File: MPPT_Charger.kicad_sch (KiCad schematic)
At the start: 119 parts, among them J1 Solar, J2 Battery, J4 INTERFACE PORT, J6 JTAG, J8 Micro_SD_Card_Det_Hirose_DM3AT, J9 IIC RTC, P1 USB-C, Q1 CSD19505KCS, Q2 CSD19505KCS, Q3 CSD19505KCS, Q4 Si2306, Q5 MMBT3904 1A, Q6 MMBT3904 1A, Q7 Si2306, U1 ACS712, U10 ADS1015, U2 B1212S, U3 AMS1117-5.0, U4 AMS1117-3.3, U5 XL7005A, U6 XL7005A, U7 IR2104, U8 ESP32, U9 CH340G

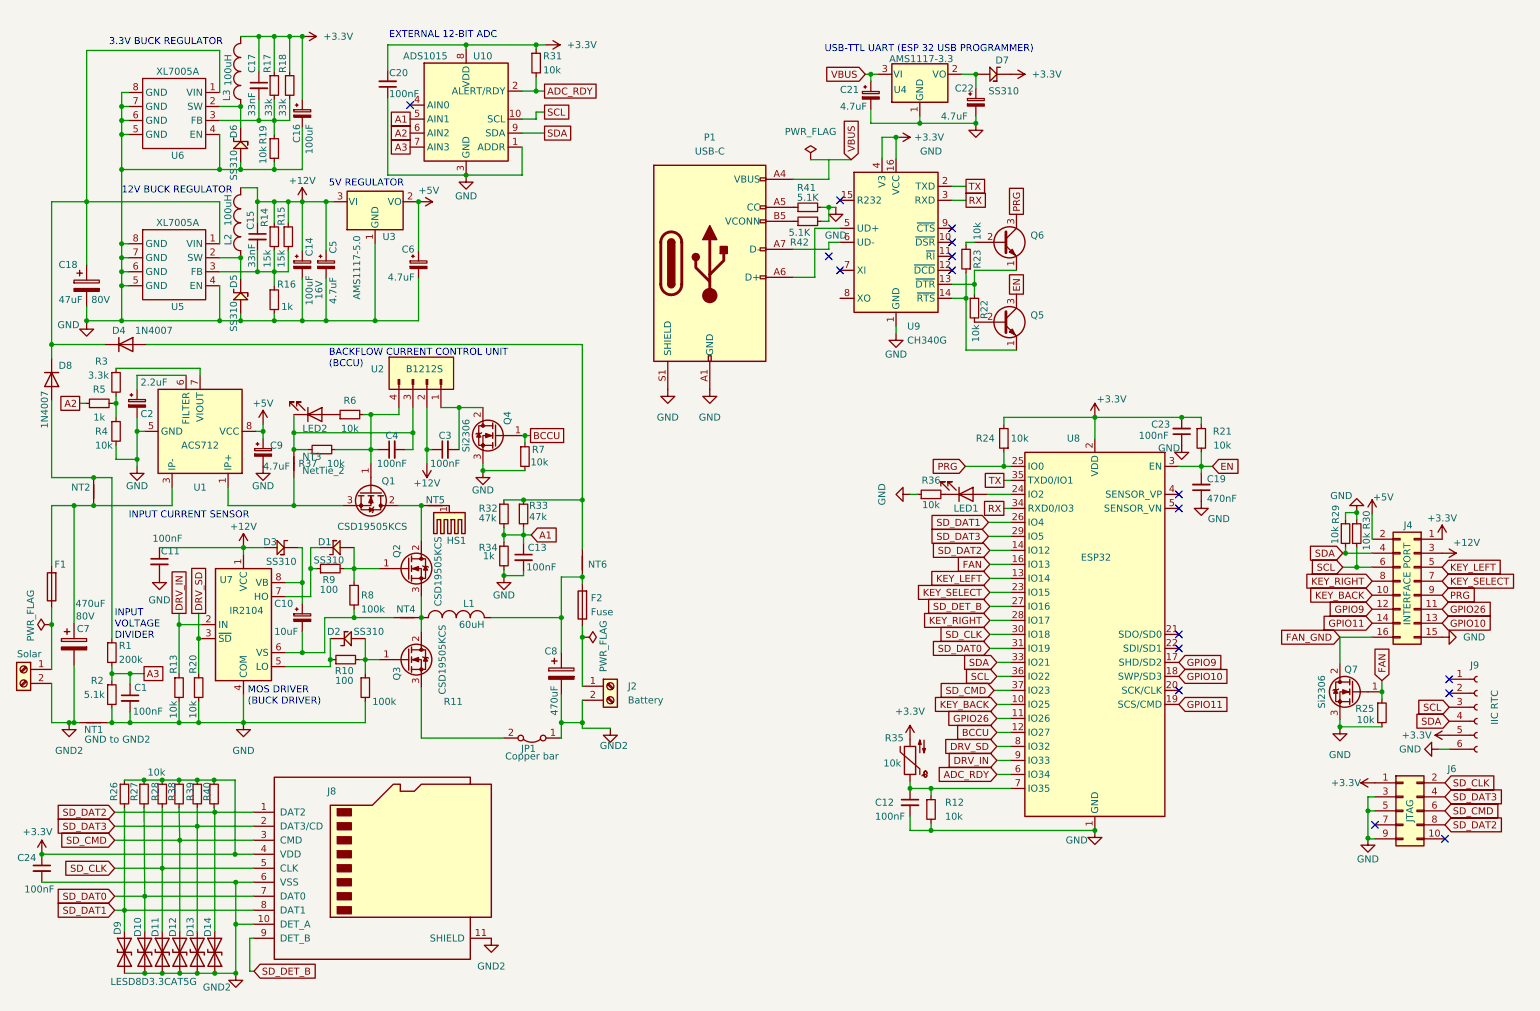
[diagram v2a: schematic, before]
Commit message: A lot of updates. Used net classes. Changed some footprints and 3D models. Corrected pinouts of connectors. Changed pins for keyboard to use same pins as JTAG connector, seemed like a useful double use that should not collide, and I am running out of GPIOs soon.
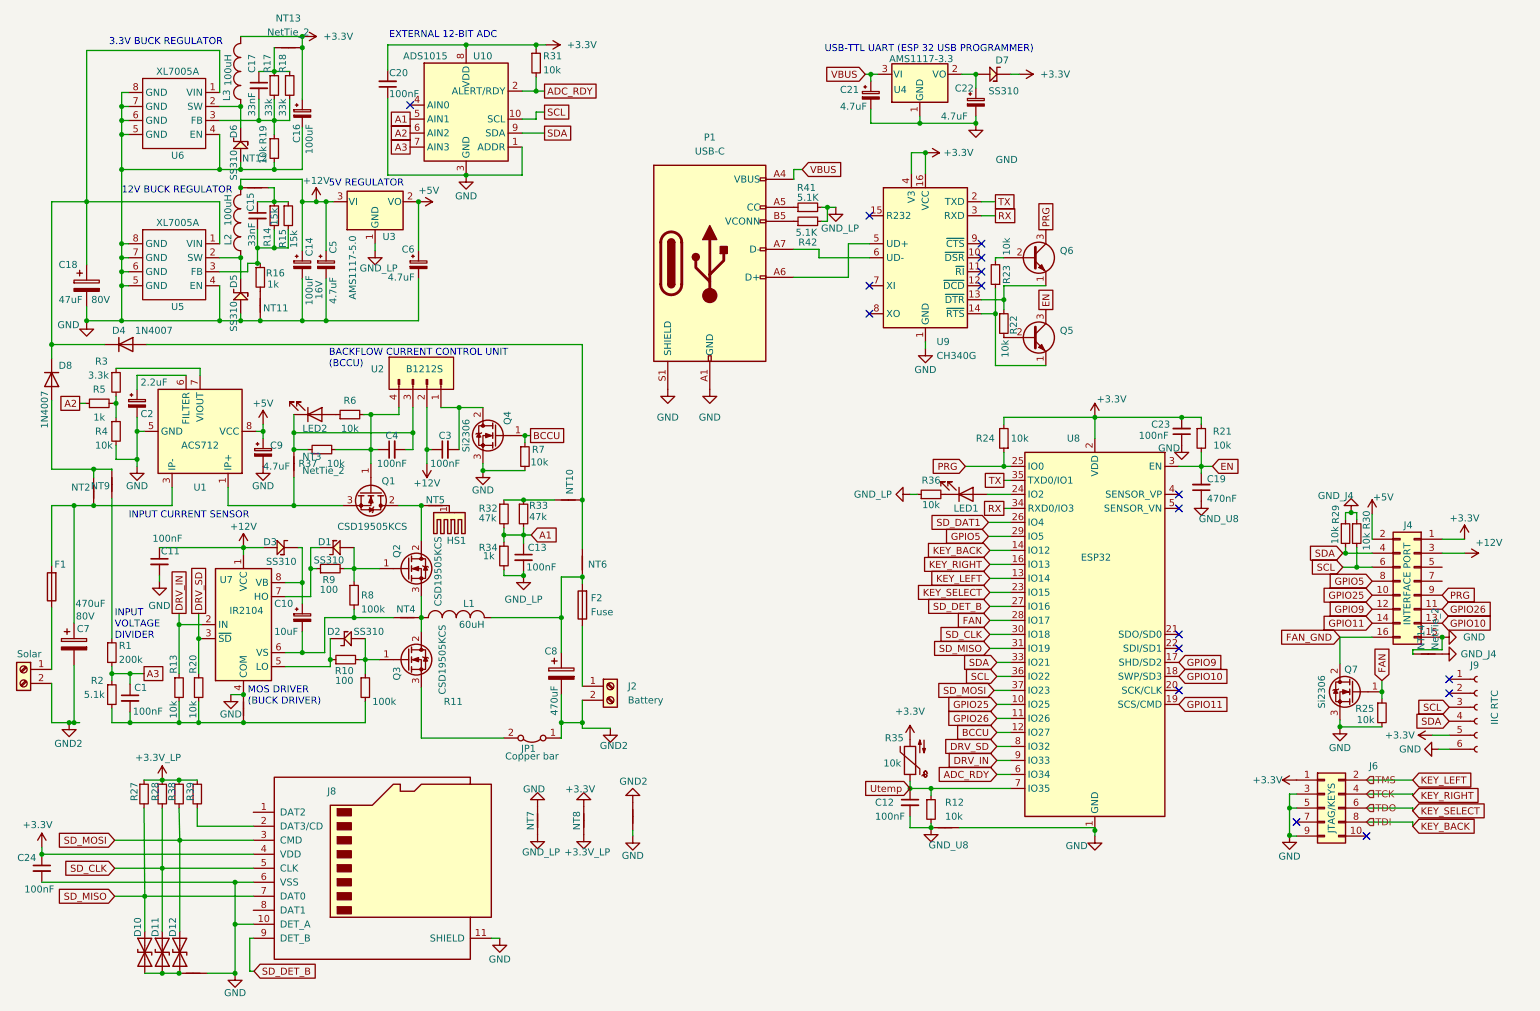
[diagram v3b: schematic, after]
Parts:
- removed D13, D14, D9: LESD8D3.3CAT5G, AA:SOD882D.kicad_mod, symbol Diode:1N62xxCA
- removed R26, R40: 10k, Resistor_SMD:R_0603_1608Metric, symbol Device:R_Small
- added NT10, NT11, NT12, NT13, NT14, NT15, NT16, NT17, NT9: NetTie_2, NetTie:NetTie-2_SMD_Pad0.5mm, symbol Device:NetTie_2
- added NT7, NT8: ~, NetTie:NetTie-2_SMD_Pad0.5mm, symbol Device:NetTie_2
- C1: JLCPCB Part (none) -> C14663 CC0603KRX7R9BB104
- C17: LCSC (none) -> C21117 CL10B333KB8NNNC; Voltage (none) -> 5V
- C6: LCSC (none) -> C1779 CL21A475KAQNNNE; Voltage (none) -> 5V
- C8: Voltage (none) -> 50V
- D4, D8: footprint Diode_SMD:D_SMB -> Diode_SMD:D_SOD-123F
- J6: value JTAG -> JTAG/KEYS
- U1: LCSC (none) -> C10681 ACS712ELCTR-20A-T
- U9: LCSC (none) -> C14267 CH340G
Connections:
- net +12V: now also NT12.1; no longer C15.1, R14.1, R15.1
- net +3.3V: now also NT13.2, NT8.2; no longer C17.1, R17.1, R18.1, R27.1, R28.1, R38.1, R39.1
- net FAN: now also U8.28 (IO17); no longer U8.16 (IO13)
- net GND: now also C24.2, J8.10 (DET_A), J8.11 (SHIELD), J8.6 (VSS), NT1.2, NT11.1, NT14.2, NT15.2, NT16.2, NT17.2, NT7.2; no longer C1.2, C12.2, C13.2, C19.1, NT1.1, R11.2, R12.2, R13.2, R16.2, R2.2, R20.2, R29.1, R30.1, R34.2, R36.1, R41.2, R42.2, U3.1 (GND)
- net GND2: now also NT1.1; no longer C24.2, D10.1 (A1), D11.1 (A1), D12.1 (A1), J8.10 (DET_A), J8.11 (SHIELD), J8.6 (VSS), NT1.2
- net KEY_BACK: now also J6.8 (Pin_8), U8.14 (IO12); no longer J4.10 (Pin_10), U8.10 (IO25)
- net KEY_LEFT: now also J6.2 (Pin_2); no longer J4.5 (Pin_5)
- net KEY_RIGHT: now also J6.4 (Pin_4), U8.16 (IO13); no longer J4.8 (Pin_8), U8.28 (IO17)
- net KEY_SELECT: now also J6.6 (Pin_6); no longer J4.7 (Pin_7)
- net SD_CLK: no longer J6.2 (Pin_2)
- net SD_DAT1: no longer J8.8 (DAT1)
- net VBUS: now also P1.A4 (VBUS), P1.A9 (VBUS), P1.B4 (VBUS), P1.B9 (VBUS)
- net Utemp: now reaches C12.1, R12.1, R35.1, U8.7 (IO35)
- net at D8.2 (A), NT2.1: now also NT9.1; no longer R1.1
- net at R32.1, R33.1: now also NT10.2; no longer D4.2 (A), NT6.2
- net SD_CMD renamed SD_MOSI
- net SD_MOSI: no longer J6.6 (Pin_6)
- net SD_DAT0 renamed SD_MISO
- removed net SD_DAT2: J6.8 (Pin_8), J8.1 (DAT2), U8.14 (IO12)
- net SD_DAT3: no longer names the net of J8.2 (DAT3/CD), R39.2
- net SD_DAT3: no longer J6.4 (Pin_4), U8.29 (IO5)
- new net: C1.2, NT17.1, R11.2, R13.2, R2.2, R20.2
- new net: C17.1, NT13.1, R17.1, R18.1
- new net: NT11.2, R16.2
- new net: C15.1, NT12.2, R14.1, R15.1
- new net: D10.1 (A1), D11.1 (A1), D12.1 (A1), NT16.1
- new net: D4.2 (A), NT10.1, NT6.2
- new net: NT9.2, R1.1
- new net +3.3V_LP: NT8.1, R27.1, R28.1, R38.1, R39.1
- new net GND_J4: NT14.1, R29.1, R30.1
- new net GND_LP: C13.2, NT7.1, R34.2, R36.1, R41.2, R42.2, U3.1 (GND)
- new net GND_U8: C12.2, C19.1, NT15.1, R12.2
- new net GPIO25: J4.10 (Pin_10), U8.10 (IO25)
- new net GPIO5: J4.8 (Pin_8), U8.29 (IO5)
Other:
- moved on the sheet: C15, J6, Q5, Q6, R14, R15, R16, R22, R23, U9

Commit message: Some Zones were wrong/missing
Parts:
- NT3: value NetTie_2 -> ~
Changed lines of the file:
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@@
 	)
 	(junction
-		(at 24.384 139.192)
-		(diameter 0)
-		(color 0 0 0 0)
-	)
-	(junction
 		(at 116.586 139.192)
 		(diameter 0)
@@
 	(wire
 		(pts
+			(xy 108.458 153.67) (xy 108.458 154.432)
+		)
+		(stroke
+			(width 0)
+			(type default)
+		)
+	)
+	(wire
+		(pts
 			(xy 65.786 44.704) (xy 65.786 53.594)
 		)
@@
 	(wire
 		(pts
+			(xy 125.73 159.258) (xy 125.73 159.766)
+		)
+		(stroke
+			(width 0)
+			(type default)
+		)
+	)
+	(wire
+		(pts
 			(xy 70.866 127.762) (xy 71.12 127.762)
 		)
@@
 	(wire
 		(pts
-			(xy 24.384 139.192) (xy 25.4 139.192)
-		)
-		(stroke
-			(width 0)
-			(type default)
-		)
-	)
-	(wire
-		(pts
 			(xy 193.04 83.82) (xy 193.04 85.09)
 		)
@@
 	(wire
 		(pts
-			(xy 60.706 16.764) (xy 60.706 21.082)
+			(xy 116.84 153.67) (xy 116.84 154.432)
 		)
 		(stroke
@@
 	(wire
 		(pts
-			(xy 56.261 178.308) (xy 56.896 178.308)
+			(xy 60.706 16.764) (xy 60.706 21.082)
 		)
 		(stroke
@@
 	(wire
 		(pts
-			(xy 33.02 54.864) (xy 34.29 54.864)
+			(xy 56.261 178.308) (xy 56.896 178.308)
 		)
 		(stroke
@@
 	(wire
 		(pts
-			(xy 102.362 98.806) (xy 105.918 98.806)
+			(xy 33.02 54.864) (xy 34.29 54.864)
 		)
 		(stroke
@@
 	(wire
 		(pts
-			(xy 261.62 133.604) (xy 261.62 134.874)
+			(xy 102.362 98.806) (xy 105.918 98.806)
 		)
 		(stroke
@@
 	(wire
 		(pts
-			(xy 125.73 158.75) (xy 125.73 159.766)
+			(xy 261.62 133.604) (xy 261.62 134.874)
 		)
 		(stroke
@@
 	(wire
 		(pts
+			(xy 125.73 153.67) (xy 125.73 154.178)
+		)
+		(stroke
+			(width 0)
+			(type default)
+		)
+	)
+	(wire
+		(pts
 			(xy 65.786 126.492) (xy 69.85 126.492)
 		)
@@
 		(length 2.54)
 		(shape round)
-		(at 26.67 17.272 0)
+		(at 116.84 154.432 90)
 		(fields_autoplaced yes)
 		(effects
@@
 		)
 		(property "Netclass" "MEDPWR"
-			(at 27.3685 14.732 0)
+			(at 114.3 153.7335 90)
 			(show_name yes)
 			(effects
@@
 		(length 2.54)
 		(shape round)
-		(at 53.34 54.864 0)
+		(at 26.67 17.272 0)
 		(fields_autoplaced yes)
 		(effects
@@
 		)
 		(property "Netclass" "MEDPWR"
-			(at 54.0385 52.324 0)
+			(at 27.3685 14.732 0)
 			(show_name yes)
 			(effects
@@
 		(length 2.54)
 		(shape round)
-		(at 116.586 129.032 270)
+		(at 53.34 54.864 0)
 		(fields_autoplaced yes)
 		(effects
@@
 				(size 1.27 1.27)
 			)
-			(justify right bottom)
+			(justify left bottom)
 		)
-		(property "Netclass" "HIPWR"
-			(at 119.126 128.3335 90)
+		(property "Netclass" "MEDPWR"
+			(at 54.0385 52.324 0)
 			(show_name yes)
 			(effects
@@
 		(length 2.54)
 		(shape round)
-		(at 256.54 123.698 180)
+		(at 116.586 129.032 270)
 		(fields_autoplaced yes)
 		(effects
@@
 			(justify right bottom)
 		)
-		(property "Netclass" "MEDPWR"
-			(at 257.2385 126.238 0)
+		(property "Netclass" "HIPWR"
+			(at 119.126 128.3335 90)
 			(show_name yes)
 			(effects
@@
 		(length 2.54)
 		(shape round)
-		(at 25.908 93.218 0)
+		(at 256.54 123.698 180)
 		(fields_autoplaced yes)
 		(effects
@@
 				(size 1.27 1.27)
 			)
-			(justify left bottom)
+			(justify right bottom)
 		)
 		(property "Netclass" "MEDPWR"
-			(at 26.6065 90.678 0)
+			(at 257.2385 126.238 0)
 			(show_name yes)
 			(effects
@@
 		(length 2.54)
 		(shape round)
-		(at 87.376 116.84 90)
+		(at 25.908 93.218 0)
 		(fields_autoplaced yes)
 		(effects
@@
 			(justify left bottom)
 		)
-		(property "Netclass" "HIPWR"
-			(at 84.836 116.1415 90)
+		(property "Netclass" "MEDPWR"
+			(at 26.6065 90.678 0)
 			(show_name yes)
 			(effects
@@
 		(length 2.54)
 		(shape round)
-		(at 87.376 99.822 0)
+		(at 87.376 116.84 90)
 		(fields_autoplaced yes)
 		(effects
@@
 		)
 		(property "Netclass" "HIPWR"
-			(at 88.0745 97.282 0)
+			(at 84.836 116.1415 90)
 			(show_name yes)
 			(effects
@@
 		(length 2.54)
 		(shape round)
-		(at 273.558 105.918 0)
+		(at 87.376 99.822 0)
 		(fields_autoplaced yes)
 		(effects
@@
 			(justify left bottom)
 		)
-		(property "Netclass" "MEDPWR"
-			(at 274.2565 103.378 0)
+		(property "Netclass" "HIPWR"
+			(at 88.0745 97.282 0)
 			(show_name yes)
 			(effects
@@
 	(symbol
 		(lib_id "Device:NetTie_2")
-		(at 125.73 156.21 270)
+		(at 125.73 156.718 270)
 		(unit 1)
 		(exclude_from_sim no)
@@
 		(dnp no)
 		(property "Reference" "NT1"
-			(at 127 156.21 0)
+			(at 127 156.718 0)
 			(effects
 				(font
@@
 		)
 		(property "Value" "GND to GND2"
-			(at 128.778 151.892 0)
+			(at 128.778 152.4 0)
 			(effects
 				(font
@@
 		)
 		(property "Footprint" "NetTie:NetTie-2_SMD_Pad0.5mm"
-			(at 125.73 156.21 0)
+			(at 125.73 156.718 0)
 			(effects
 				(font
@@
 		)
 		(property "Datasheet" "~"
-			(at 125.73 156.21 0)
+			(at 125.73 156.718 0)
 			(effects
 				(font
@@
 		)
 		(property "Description" "Net tie, 2 pins"
-			(at 125.73 156.21 0)
+			(at 125.73 156.718 0)
 			(effects
 				(font
@@
 		(on_board yes)
 		(dnp no)
-		(fields_autoplaced yes)
 		(property "Reference" "NT13"
-			(at 63.246 11.43 0)
+			(at 62.738 15.748 0)
 			(effects
 				(font
 					(size 1.27 1.27)
 				)
+				(hide yes)
 			)
 		)
@@
 					(size 1.27 1.27)
 				)
+				(hide yes)
 			)
 		)
@@
 					(size 1.27 1.27)
 				)
+				(hide yes)
 			)
 		)
@@
 					(size 1.27 1.27)
 				)
+				(hide yes)
 			)
 		)
@@
 	(symbol
 		(lib_id "power:GND2")
-		(at 116.84 154.432 180)
+		(at 116.84 153.67 180)
 		(unit 1)
 		(exclude_from_sim no)
@@
 		(dnp no)
 		(property "Reference" "#PWR016"
-			(at 116.84 148.082 0)
+			(at 116.84 147.32 0)
 			(effects
 				(font
@@
 		)
 		(property "Value" "+3.3V"
-			(at 116.205 151.257 0)
+			(at 116.205 150.495 0)
 			(effects
 				(font
@@
 		)
 		(property "Footprint" ""
-			(at 116.84 154.432 0)
+			(at 116.84 153.67 0)
 			(effects
 				(font
@@
 		)
 		(property "Datasheet" ""
-			(at 116.84 154.432 0)
+			(at 116.84 153.67 0)
 			(effects
 				(font
@@
 		)
 		(property "Description" ""
-			(at 116.84 154.432 0)
+			(at 116.84 153.67 0)
 			(effects
 				(font
@@
 					(size 1.27 1.27)
 				)
+				(hide yes)
 			)
 		)
@@
 		(fields_autoplaced yes)
 		(property "Reference" "NT3"
-			(at 65.786 90.9319 90)
+			(at 66.04 91.5669 90)
 			(effects
 				(font
@@
 				)
 				(justify right)
+				(hide yes)
 			)
 		)
-		(property "Value" "NetTie_2"
-			(at 65.786 93.4719 90)
+		(property "Value" "~"
+			(at 66.04 92.202 90)
 			(effects
 				(font
@@
 	(symbol
 		(lib_id "power:GND2")
-		(at 108.458 154.432 180)
+		(at 108.458 153.67 180)
 		(unit 1)
 		(exclude_from_sim no)
@@
 		(dnp no)
 		(property "Reference" "#PWR013"
-			(at 108.458 148.082 0)
+			(at 108.458 147.32 0)
 			(effects
 				(font
@@
 		)
 		(property "Value" "GND"
-			(at 107.823 151.257 0)
+			(at 107.823 150.495 0)
 			(effects
 				(font
@@
 		)
 		(property "Footprint" ""
-			(at 108.458 154.432 0)
+			(at 108.458 153.67 0)
 			(effects
 				(font
@@
 		)
 		(property "Datasheet" ""
-			(at 108.458 154.432 0)
+			(at 108.458 153.67 0)
 			(effects
 				(font
@@
 		)
 		(property "Description" ""
-			(at 108.458 154.432 0)
+			(at 108.458 153.67 0)
 			(effects
 				(font
@@
 				)
 				(justify right)
+				(hide yes)
 			)
 		)
@@
 					(size 1.27 1.27)
 				)
+				(hide yes)
 			)
 		)

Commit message: USB-C corrected- I hope Moved more parts topside again
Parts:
- removed D7: SS310, Diode_SMD:D_SMB, symbol footprint:SS310
- removed P1: USB-C, Connector_USB:USB_C_Receptacle_GCT_USB4125-xx-x_6P_TopMnt_Horizontal, symbol Connector:USB_C_Plug_USB2.0
- added P1: USB_C_Receptacle_USB2.0_16P, Connector_USB:USB_C_Receptacle_GCT_USB4105-xx-A_16P_TopMnt_Horizontal, symbol Connector:USB_C_Receptacle_USB2.0_16P
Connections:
- net +3.3V: now also C22.1, U4.2 (VO)
- net GND: now also P1.A1 (GND), P1.A12 (GND), P1.B1 (GND), P1.B12 (GND), P1.S1 (SHIELD)
- net VBUS: now also P1.A4 (VBUS), P1.A9 (VBUS), P1.B4 (VBUS), P1.B9 (VBUS)
- net at R42.1: now also P1.B5 (CC2)
- net at R41.1: now also P1.A5 (CC1)
- net at U9.5 (UD+): now also P1.A6 (D+), P1.B6 (D+)
- net at U9.6 (UD-): now also P1.A7 (D-), P1.B7 (D-)
- no-connect marks 17 -> 19
